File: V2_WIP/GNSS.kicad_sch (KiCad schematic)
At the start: 12 parts, among them J301 USB_B_Micro, U301 USBLC6-2SC6, U401 NEO-M9N

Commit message: minor schematic changes
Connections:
- net GNSS_RXD is gone; now on net RxD: TP402.1
- net GNSS_TXD is gone; now on net TxD: TP401.1
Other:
- moved on the sheet: C401, C402, J301, TP401, TP402, U301

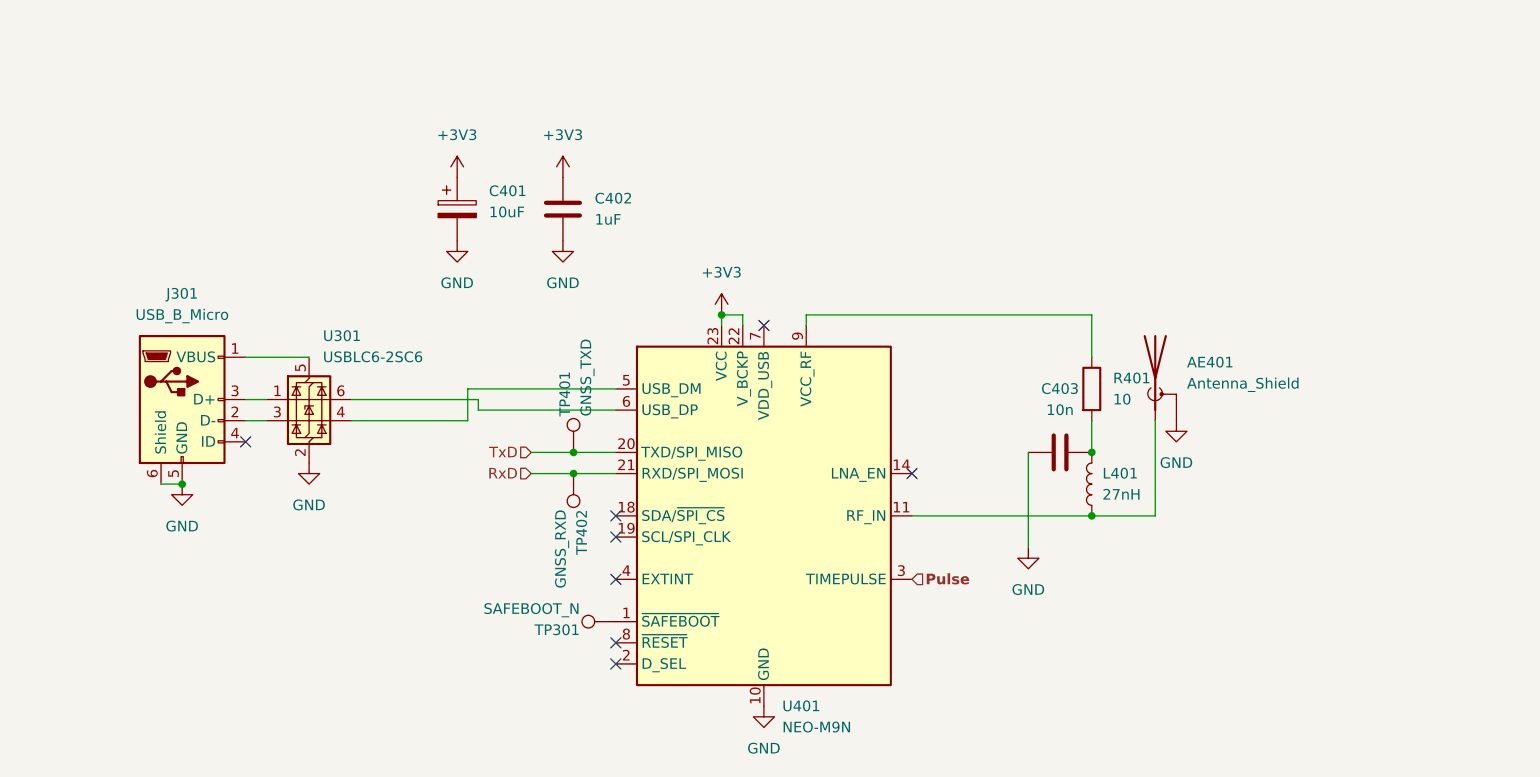
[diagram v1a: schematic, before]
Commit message: switched esp modul symbol for esp sheet
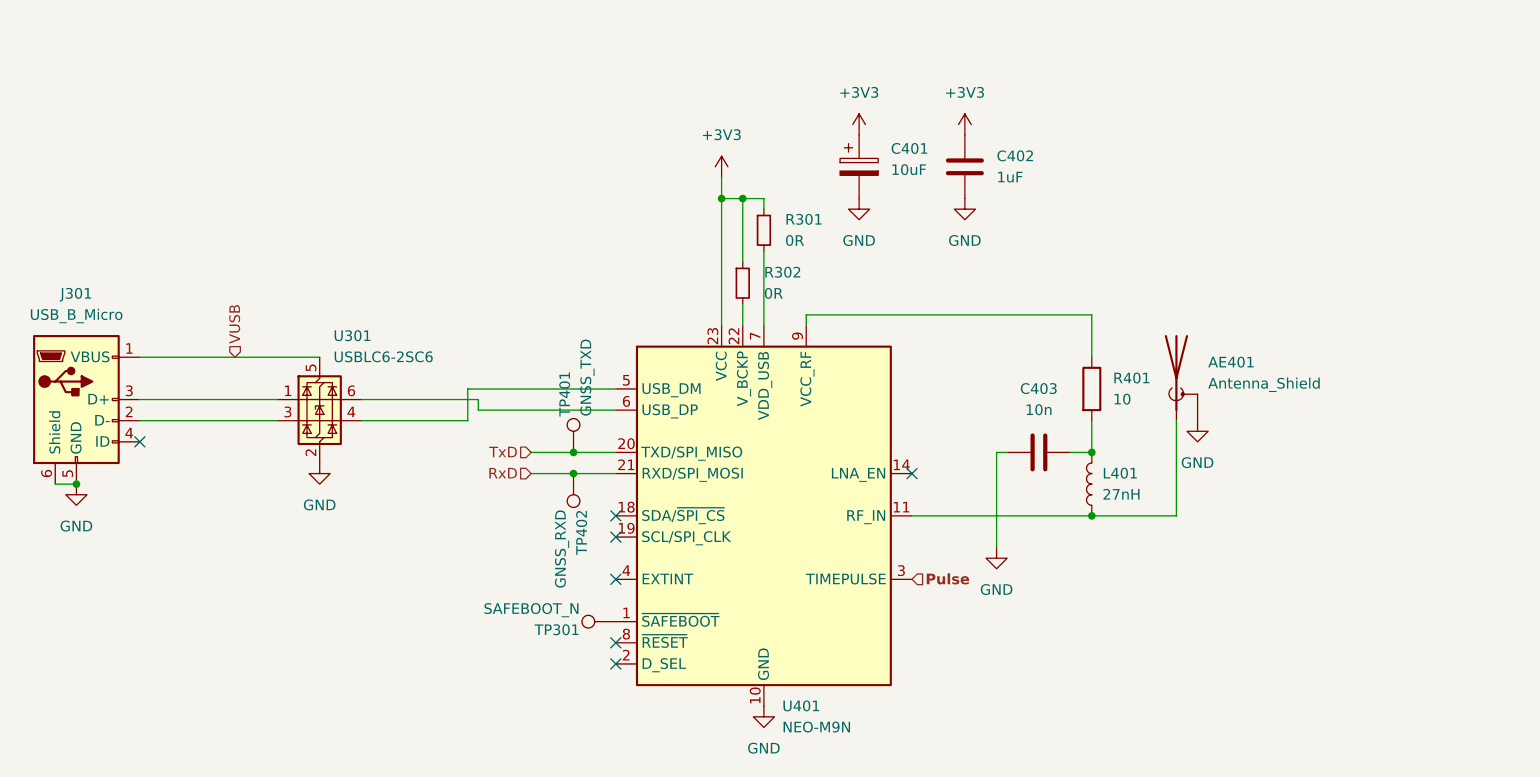
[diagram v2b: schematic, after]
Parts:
- added R301, R302: 0R, Resistor_SMD:R_0603_1608Metric_Pad0.98x0.95mm_HandSolder, symbol Device:R_Small
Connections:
- net +3V3: now also R301.1, R302.1; no longer U401.22 (V_BCKP)
- net VUSB: now reaches J301.1 (VBUS), U301.5 (VBUS)
- net at U401.7 (VDD_USB): now also R301.2
- new net: R302.2, U401.22 (V_BCKP)
- no-connect marks 8 -> 7
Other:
- moved on the sheet: AE401, C401, C402, C403, J301, U301

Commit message: added LED indicators, light sensor, changed to CC 7seg displays
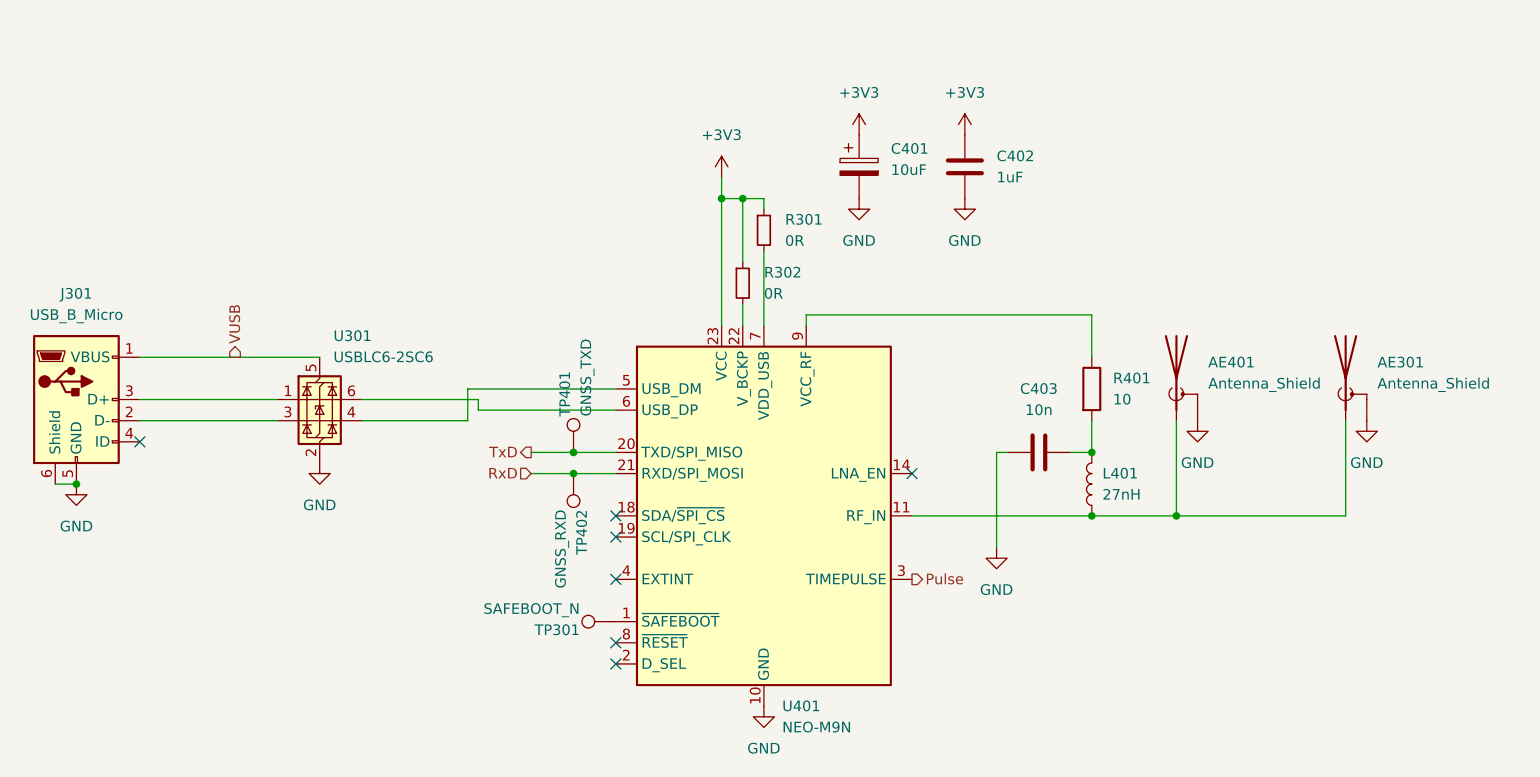
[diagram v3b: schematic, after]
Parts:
- added AE301: Antenna_Shield, Connector_Coaxial:U.FL_Molex_MCRF_73412-0110_Vertical, symbol Device:Antenna_Shield
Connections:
- net GND: now also AE301.2 (Shield)
- net at AE401.1 (A), L401.1, U401.11 (RF_IN): now also AE301.1 (A)
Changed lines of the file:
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@@
+	)
+	(junction
+		(at 189.23 107.95)
+		(diameter 0)
+		(color 0 0 0 0)
 	)
 	(junction
@@
 	(wire
 		(pts
+			(xy 189.23 107.95) (xy 209.55 107.95)
+		)
+		(stroke
+			(width 0)
+			(type default)
+		)
+	)
+	(wire
+		(pts
 			(xy 134.62 69.85) (xy 134.62 85.09)
 		)
@@
 		(pts
 			(xy 137.16 82.55) (xy 137.16 85.09)
+		)
+		(stroke
+			(width 0)
+			(type default)
+		)
+	)
+	(wire
+		(pts
+			(xy 209.55 107.95) (xy 209.55 96.52)
 		)
 		(stroke
@@
 	)
 	(hierarchical_label "Pulse"
-		(shape input)
+		(shape output)
 		(at 157.48 115.57 0)
 		(fields_autoplaced yes)
@@
 			(font
 				(size 1.27 1.27)
-				(bold yes)
 			)
 			(justify left)
@@
 	)
 	(hierarchical_label "TxD"
-		(shape input)
+		(shape output)
 		(at 111.76 100.33 180)
 		(fields_autoplaced yes)
@@
 	)
 	(hierarchical_label "VUSB"
-		(shape input)
+		(shape output)
 		(at 76.2 88.9 90)
 		(fields_autoplaced yes)
@@
 				(path "/00526ddc-5304-4072-af1e-192a9e7e83da/5cdf5b9a-bc05-4fbb-ac1a-8c1a969964f2"
 					(reference "L401")
+					(unit 1)
+				)
+			)
+		)
+	)
+	(symbol
+		(lib_id "power:GND")
+		(at 212.09 96.52 0)
+		(unit 1)
+		(exclude_from_sim no)
+		(in_bom yes)
+		(on_board yes)
+		(dnp no)
+		(fields_autoplaced yes)
+		(property "Reference" "#PWR0303"
+			(at 212.09 102.87 0)
+			(effects
+				(font
+					(size 1.27 1.27)
+				)
+				(hide yes)
+			)
+		)
+		(property "Value" "GND"
+			(at 212.09 101.6 0)
+			(effects
+				(font
+					(size 1.27 1.27)
+				)
+			)
+		)
+		(property "Footprint" ""
+			(at 212.09 96.52 0)
+			(effects
+				(font
+					(size 1.27 1.27)
+				)
+				(hide yes)
+			)
+		)
+		(property "Datasheet" ""
+			(at 212.09 96.52 0)
+			(effects
+				(font
+					(size 1.27 1.27)
+				)
+				(hide yes)
+			)
+		)
+		(property "Description" "Power symbol creates a global label with name \"GND\" , ground"
+			(at 212.09 96.52 0)
+			(effects
+				(font
+					(size 1.27 1.27)
+				)
+				(hide yes)
+			)
+		)
+		(pin "1"
+		)
+		(instances
+			(project "gps"
+				(path "/00526ddc-5304-4072-af1e-192a9e7e83da/5cdf5b9a-bc05-4fbb-ac1a-8c1a969964f2"
+					(reference "#PWR0303")
 					(unit 1)
 				)
@@
 					(unit 1)
 				)
+			)
+		)
+	)
+	(symbol
+		(lib_id "Device:Antenna_Shield")
+		(at 209.55 91.44 0)
+		(unit 1)
+		(exclude_from_sim no)
+		(in_bom yes)
+		(on_board yes)
+		(dnp no)
+		(fields_autoplaced yes)
+		(property "Reference" "AE301"
+			(at 213.36 89.5349 0)
+			(effects
+				(font
+					(size 1.27 1.27)
+				)
+				(justify left)
+			)
+		)
+		(property "Value" "Antenna_Shield"
+			(at 213.36 92.0749 0)
+			(effects
+				(font
+					(size 1.27 1.27)
+				)
+				(justify left)
+			)
+		)
+		(property "Footprint" "Connector_Coaxial:U.FL_Molex_MCRF_73412-0110_Vertical"
+			(at 209.55 88.9 0)
+			(effects
+				(font
+					(size 1.27 1.27)
+				)
+				(hide yes)
+			)
+		)
+		(property "Datasheet" "~"
+			(at 209.55 88.9 0)
+			(effects
+				(font
+					(size 1.27 1.27)
+				)
+				(hide yes)
+			)
+		)
+		(property "Description" "Antenna with extra pin for shielding"
+			(at 209.55 91.44 0)
+			(effects
+				(font
+					(size 1.27 1.27)
+				)
+				(hide yes)
+			)
+		)
+		(pin "1"
+		)
+		(pin "2"
+		)
+		(instances
+			(project "gps"
+				(path "/00526ddc-5304-4072-af1e-192a9e7e83da/5cdf5b9a-bc05-4fbb-ac1a-8c1a969964f2"
+					(reference "AE301")
+					(unit 1)
+				)

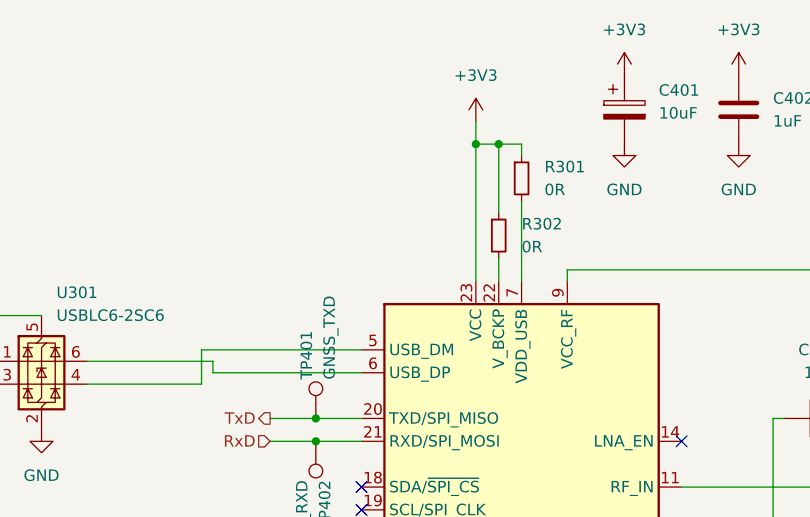
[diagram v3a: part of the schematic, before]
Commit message: added battery monitoring circuits
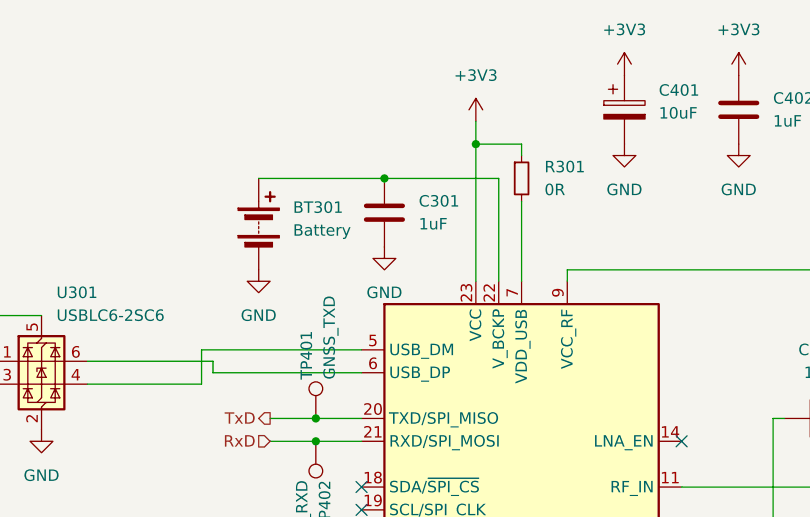
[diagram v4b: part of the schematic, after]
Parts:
- removed R302: 0R, Resistor_SMD:R_0603_1608Metric_Pad0.98x0.95mm_HandSolder, symbol Device:R_Small
- added BT301: Battery, Battery:BatteryHolder_MPD_BC2003_1x2032, symbol Device:Battery
- added C301: 1uF, Capacitor_SMD:C_0603_1608Metric_Pad1.08x0.95mm_HandSolder, symbol Device:C
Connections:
- net GND: now also BT301.2 (-), C301.2
- net at U401.22 (V_BCKP): now also BT301.1 (+), C301.1
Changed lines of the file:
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@@
-	)
-	(junction
-		(at 137.16 69.85)
-		(diameter 0)
-		(color 0 0 0 0)
 	)
 	(junction
@@
 		(color 0 0 0 0)
 	)
+	(junction
+		(at 124.46 73.66)
+		(diameter 0)
+		(color 0 0 0 0)
+	)
 	(no_connect
 		(at 121.92 115.57)
@@
 	(wire
 		(pts
-			(xy 139.7 69.85) (xy 137.16 69.85)
-		)
-		(stroke
-			(width 0)
-			(type default)
-		)
-	)
-	(wire
-		(pts
 			(xy 157.48 107.95) (xy 179.07 107.95)
 		)
@@
 	(wire
 		(pts
+			(xy 110.49 73.66) (xy 124.46 73.66)
+		)
+		(stroke
+			(width 0)
+			(type default)
+		)
+	)
+	(wire
+		(pts
 			(xy 179.07 107.95) (xy 189.23 107.95)
 		)
@@
 	(wire
 		(pts
+			(xy 124.46 73.66) (xy 137.16 73.66)
+		)
+		(stroke
+			(width 0)
+			(type default)
+		)
+	)
+	(wire
+		(pts
 			(xy 167.64 100.33) (xy 168.91 100.33)
 		)
@@
 	(wire
 		(pts
+			(xy 137.16 73.66) (xy 137.16 85.09)
+		)
+		(stroke
+			(width 0)
+			(type default)
+		)
+	)
+	(wire
+		(pts
 			(xy 189.23 107.95) (xy 209.55 107.95)
 		)
@@
 	(wire
 		(pts
-			(xy 134.62 69.85) (xy 137.16 69.85)
+			(xy 134.62 69.85) (xy 139.7 69.85)
 		)
 		(stroke
@@
 	(wire
 		(pts
-			(xy 137.16 69.85) (xy 137.16 77.47)
-		)
-		(stroke
-			(width 0)
-			(type default)
-		)
-	)
-	(wire
-		(pts
 			(xy 144.78 83.82) (xy 144.78 85.09)
-		)
-		(stroke
-			(width 0)
-			(type default)
-		)
-	)
-	(wire
-		(pts
-			(xy 137.16 82.55) (xy 137.16 85.09)
 		)
 		(stroke
@@
 	)
 	(symbol
+		(lib_id "power:GND")
+		(at 110.49 83.82 0)
+		(unit 1)
+		(exclude_from_sim no)
+		(in_bom yes)
+		(on_board yes)
+		(dnp no)
+		(fields_autoplaced yes)
+		(property "Reference" "#PWR0304"
+			(at 110.49 90.17 0)
+			(effects
+				(font
+					(size 1.27 1.27)
+				)
+				(hide yes)
+			)
+		)
+		(property "Value" "GND"
+			(at 110.49 88.9 0)
+			(effects
+				(font
+					(size 1.27 1.27)
+				)
+			)
+		)
+		(property "Footprint" ""
+			(at 110.49 83.82 0)
+			(effects
+				(font
+					(size 1.27 1.27)
+				)
+				(hide yes)
+			)
+		)
+		(property "Datasheet" ""
+			(at 110.49 83.82 0)
+			(effects
+				(font
+					(size 1.27 1.27)
+				)
+				(hide yes)
+			)
+		)
+		(property "Description" "Power symbol creates a global label with name \"GND\" , ground"
+			(at 110.49 83.82 0)
+			(effects
+				(font
+					(size 1.27 1.27)
+				)
+				(hide yes)
+			)
+		)
+		(pin "1"
+		)
+		(instances
+			(project "gps"
+				(path "/00526ddc-5304-4072-af1e-192a9e7e83da/5cdf5b9a-bc05-4fbb-ac1a-8c1a969964f2"
+					(reference "#PWR0304")
+					(unit 1)
+				)
+			)
+		)
+	)
+	(symbol
 		(lib_id "Device:Antenna_Shield")
 		(at 209.55 91.44 0)
@@
 	)
 	(symbol
+		(lib_id "Device:C")
+		(at 124.46 77.47 0)
+		(unit 1)
+		(exclude_from_sim no)
+		(in_bom yes)
+		(on_board yes)
+		(dnp no)
+		(fields_autoplaced yes)
+		(property "Reference" "C301"
+			(at 128.27 76.1999 0)
+			(effects
+				(font
+					(size 1.27 1.27)
+				)
+				(justify left)
+			)
+		)
+		(property "Value" "1uF"
+			(at 128.27 78.7399 0)
+			(effects
+				(font
+					(size 1.27 1.27)
+				)
+				(justify left)
+			)
+		)
+		(property "Footprint" "Capacitor_SMD:C_0603_1608Metric_Pad1.08x0.95mm_HandSolder"
+			(at 125.4252 81.28 0)
+			(effects
+				(font
+					(size 1.27 1.27)
+				)
+				(hide yes)
+			)
+		)
+		(property "Datasheet" "~"
+			(at 124.46 77.47 0)
+			(effects
+				(font
+					(size 1.27 1.27)
+				)
+				(hide yes)
+			)
+		)
+		(property "Description" "Unpolarized capacitor"
+			(at 124.46 77.47 0)
+			(effects
+				(font
+					(size 1.27 1.27)
+				)
+				(hide yes)
+			)
+		)
+		(pin "1"
+		)
+		(pin "2"
+		)
+		(instances
+			(project "gps"
+				(path "/00526ddc-5304-4072-af1e-192a9e7e83da/5cdf5b9a-bc05-4fbb-ac1a-8c1a969964f2"
+					(reference "C301")
+					(unit 1)
+				)
+			)
+		)
+	)
+	(symbol
 		(lib_id "power:GND")
 		(at 191.77 96.52 0)
@@
 	)
 	(symbol
-		(lib_id "Device:R_Small")
-		(at 137.16 80.01 0)
-		(unit 1)
-		(exclude_from_sim no)
-		(in_bom yes)
-		(on_board yes)
-		(dnp no)
-		(fields_autoplaced yes)
-		(property "Reference" "R302"
-			(at 139.7 78.7399 0)
-			(effects
-				(font
-					(size 1.27 1.27)
-				)
-				(justify left)
-			)
-		)
-		(property "Value" "0R"
-			(at 139.7 81.2799 0)
-			(effects
-				(font
-					(size 1.27 1.27)
-				)
-				(justify left)
-			)
-		)
-		(property "Footprint" "Resistor_SMD:R_0603_1608Metric_Pad0.98x0.95mm_HandSolder"
-			(at 137.16 80.01 0)
-			(effects
-				(font
-					(size 1.27 1.27)
-				)
-				(hide yes)
-			)
-		)
-		(property "Datasheet" "~"
-			(at 137.16 80.01 0)
-			(effects
-				(font
-					(size 1.27 1.27)
-				)
-				(hide yes)
-			)
-		)
-		(property "Description" "Resistor, small symbol"
-			(at 137.16 80.01 0)
-			(effects
-				(font
-					(size 1.27 1.27)
-				)
-				(hide yes)
-			)
-		)
-		(pin "2"
-		)
-		(pin "1"
-		)
-		(instances
-			(project "gps"
-				(path "/00526ddc-5304-4072-af1e-192a9e7e83da/5cdf5b9a-bc05-4fbb-ac1a-8c1a969964f2"
-					(reference "R302")
-					(unit 1)
-				)
-			)
-		)
-	)
-	(symbol
 		(lib_id "power:GND")
 		(at 167.64 111.76 0)
@@
 	)
 	(symbol
+		(lib_id "power:GND")
+		(at 124.46 81.28 0)
+		(unit 1)
+		(exclude_from_sim no)
+		(in_bom yes)
+		(on_board yes)
+		(dnp no)
+		(fields_autoplaced yes)
+		(property "Reference" "#PWR0305"
+			(at 124.46 87.63 0)
+			(effects
+				(font
+					(size 1.27 1.27)
+				)
+				(hide yes)
+			)
+		)
+		(property "Value" "GND"
+			(at 124.46 86.36 0)
+			(effects
+				(font
+					(size 1.27 1.27)
+				)
+			)
+		)
+		(property "Footprint" ""
+			(at 124.46 81.28 0)
+			(effects
+				(font
+					(size 1.27 1.27)
+				)
+				(hide yes)
+			)
+		)
+		(property "Datasheet" ""
+			(at 124.46 81.28 0)
+			(effects
+				(font
+					(size 1.27 1.27)
+				)
+				(hide yes)
+			)
+		)
+		(property "Description" "Power symbol creates a global label with name \"GND\" , ground"
+			(at 124.46 81.28 0)
+			(effects
+				(font
+					(size 1.27 1.27)
+				)
+				(hide yes)
+			)
+		)
+		(pin "1"
+		)
+		(instances
+			(project "gps"
+				(path "/00526ddc-5304-4072-af1e-192a9e7e83da/5cdf5b9a-bc05-4fbb-ac1a-8c1a969964f2"
+					(reference "#PWR0305")
+					(unit 1)
+				)
+			)
+		)
+	)
+	(symbol
 		(lib_id "Device:C")
 		(at 172.72 100.33 90)
@@
 					(unit 1)
 				)
+			)
+		)
+	)
+	(symbol
+		(lib_id "Device:Battery")
+		(at 110.49 78.74 0)
+		(unit 1)
+		(exclude_from_sim no)
+		(in_bom yes)
+		(on_board yes)
+		(dnp no)
+		(fields_autoplaced yes)
+		(property "Reference" "BT301"
+			(at 114.3 76.8984 0)
+			(effects
+				(font
+					(size 1.27 1.27)
+				)
+				(justify left)
+			)
+		)
+		(property "Value" "Battery"
+			(at 114.3 79.4384 0)
+			(effects
+				(font
+					(size 1.27 1.27)
+				)
+				(justify left)
+			)
+		)
+		(property "Footprint" "Battery:BatteryHolder_MPD_BC2003_1x2032"
+			(at 110.49 77.216 90)
+			(effects
+				(font
+					(size 1.27 1.27)
+				)
+				(hide yes)
+			)
+		)
+		(property "Datasheet" "~"
+			(at 110.49 77.216 90)
+			(effects
+				(font
+					(size 1.27 1.27)
+				)
+				(hide yes)
+			)
+		)
+		(property "Description" "Multiple-cell battery"
+			(at 110.49 78.74 0)
+			(effects
+				(font
+					(size 1.27 1.27)
+				)
+				(hide yes)
+			)
+		)
+		(pin "1"
+		)
+		(pin "2"
+		)
+		(instances
+			(project "gps"
+				(path "/00526ddc-5304-4072-af1e-192a9e7e83da/5cdf5b9a-bc05-4fbb-ac1a-8c1a969964f2"
+					(reference "BT301")
+					(unit 1)
+				)
